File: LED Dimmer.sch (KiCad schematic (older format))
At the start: 78 parts, among them P1 Red Load, P2 Green Load, P3 Blue Load, P4 PWR, Q1 TIP31C, Q2 TIP31C, Q3 TIP31C, Q4 Q_PNP_EBC, Q5 Q_PNP_EBC, Q6 Q_NPN_EBC, SW1 SW_SPDT, SW10 SW_SPDT, SW11 SW_SPDT, SW12 SW_SPDT, SW2 SW_SPDT, SW3 SW_SPDT, SW4 SW_SPDT, SW5 SW_SPDT, SW6 SW_SPDT, SW7 SW_SPDT, SW8 SW_SPDT, SW9 SW_SPDT, U1 LM358, U2 LM358, U3 LM358, U4 LM555N

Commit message: Routed
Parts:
- R7: Power (none) -> 1/4W
- TP1, TP2, TP3, TP4, TP5, TP6, TP7, TP8: footprint LED Dimmer Footprints:Measurement_Point_Round-SMD-Pad_Big -> LED Dimmer Footprints:test_pt_alt
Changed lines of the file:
@@
 F 2 "LED Dimmer Footprints:R_Axial" V 2530 1900 50  0001 C CNN
 F 3 "" H 2600 1900 50  0000 C CNN
+F 4 "1/4W" V 2600 1900 60  0001 C CNN "Power"
 	1    2600 1900
 	0    1    1    0
@@
 F 0 "TP7" H 9000 2700 50  0000 C BNN
 F 1 "TEST" H 9000 2650 50  0000 C CNN
-F 2 "LED Dimmer Footprints:Measurement_Point_Round-SMD-Pad_Big" H 9000 2400 50  0001 C CNN
+F 2 "LED Dimmer Footprints:test_pt_alt" H 9000 2400 50  0001 C CNN
 F 3 "" H 9000 2400 50  0001 C CNN
 	1    9000 2400
@@
 F 0 "TP8" H 10400 5300 50  0000 C BNN
 F 1 "TEST" H 10400 5250 50  0000 C CNN
-F 2 "LED Dimmer Footprints:Measurement_Point_Round-SMD-Pad_Big" H 10400 5000 50  0001 C CNN
+F 2 "LED Dimmer Footprints:test_pt_alt" H 10400 5000 50  0001 C CNN
 F 3 "" H 10400 5000 50  0001 C CNN
 	1    10400 5000
@@
 F 0 "TP3" H 4050 6800 50  0000 C BNN
 F 1 "TEST" H 4050 6750 50  0000 C CNN
-F 2 "LED Dimmer Footprints:Measurement_Point_Round-SMD-Pad_Big" H 4050 6500 50  0001 C CNN
+F 2 "LED Dimmer Footprints:test_pt_alt" H 4050 6500 50  0001 C CNN
 F 3 "" H 4050 6500 50  0001 C CNN
 	1    4050 6500
@@
 F 0 "TP2" H 4050 4650 50  0000 C BNN
 F 1 "TEST" H 4050 4600 50  0000 C CNN
-F 2 "LED Dimmer Footprints:Measurement_Point_Round-SMD-Pad_Big" H 4050 4350 50  0001 C CNN
+F 2 "LED Dimmer Footprints:test_pt_alt" H 4050 4350 50  0001 C CNN
 F 3 "" H 4050 4350 50  0001 C CNN
 	1    4050 4350
@@
 F 0 "TP1" H 3900 1800 50  0000 C BNN
 F 1 "TEST" H 3900 1750 50  0000 C CNN
-F 2 "LED Dimmer Footprints:Measurement_Point_Round-SMD-Pad_Big" H 3900 1500 50  0001 C CNN
+F 2 "LED Dimmer Footprints:test_pt_alt" H 3900 1500 50  0001 C CNN
 F 3 "" H 3900 1500 50  0001 C CNN
 	1    3900 1500
@@
 F 0 "TP4" H 6150 1550 50  0000 C BNN
 F 1 "TEST" H 6150 1500 50  0000 C CNN
-F 2 "LED Dimmer Footprints:Measurement_Point_Round-SMD-Pad_Big" H 6150 1250 50  0001 C CNN
+F 2 "LED Dimmer Footprints:test_pt_alt" H 6150 1250 50  0001 C CNN
 F 3 "" H 6150 1250 50  0001 C CNN
 	1    6150 1250
@@
 F 0 "TP5" H 6200 3750 50  0000 C BNN
 F 1 "TEST" H 6200 3700 50  0000 C CNN
-F 2 "LED Dimmer Footprints:Measurement_Point_Round-SMD-Pad_Big" H 6200 3450 50  0001 C CNN
+F 2 "LED Dimmer Footprints:test_pt_alt" H 6200 3450 50  0001 C CNN
 F 3 "" H 6200 3450 50  0001 C CNN
 	1    6200 3450
@@
 F 0 "TP6" H 6200 5900 50  0000 C BNN
 F 1 "TEST" H 6200 5850 50  0000 C CNN
-F 2 "LED Dimmer Footprints:Measurement_Point_Round-SMD-Pad_Big" H 6200 5600 50  0001 C CNN
+F 2 "LED Dimmer Footprints:test_pt_alt" H 6200 5600 50  0001 C CNN
 F 3 "" H 6200 5600 50  0001 C CNN
 	1    6200 5600

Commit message: Renamed library for compatibility with 3D viewer
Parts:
- C1: footprint LED Dimmer Footprints:C_Disc -> led_dimmer_footprints:C_Disc
- D1: footprint LED Dimmer Footprints:LED_D5.0mm-4 -> led_dimmer_footprints:LED_D5.0mm-4
- D2: footprint LED Dimmer Footprints:D_axial -> led_dimmer_footprints:D_axial
- P1, P2, P3, P4: footprint LED Dimmer Footprints:2.1ID_5.5OD_SIDE_MOUNT_JACK -> led_dimmer_footprints:2.1ID_5.5OD_SIDE_MOUNT_JACK
- Q1, Q2, Q3: footprint LED Dimmer Footprints:TO-220_Vertical -> led_dimmer_footprints:TO-220_Vertical
- Q4, Q5, Q6: footprint LED Dimmer Footprints:TO-92_Molded_Wide -> led_dimmer_footprints:TO-92_Molded_Wide
- R1, R10, R11, R12, R13, R14, R15, R16, R17, R18, R19, R2, R20, R21, R22, R23, R24, R25, R26, R27, R28, R29, R3, R30, R31, R32, R33, R34, R35, R36, R37, R38, R39, R4, R40, R5, R6, R7, R8, R9: footprint LED Dimmer Footprints:R_Axial -> led_dimmer_footprints:R_Axial
- RV1: footprint LED Dimmer Footprints:POT_UM_296RE -> led_dimmer_footprints:POT_UM_296RE
- SW1, SW10, SW11, SW12, SW2, SW3, SW4, SW5, SW6, SW7, SW8, SW9: footprint LED Dimmer Footprints:SW_SPDT_PCBPM -> led_dimmer_footprints:SW_SPDT_PCBPM
- TP1, TP2, TP3, TP4, TP5, TP6, TP7, TP8: footprint LED Dimmer Footprints:test_pt_alt -> led_dimmer_footprints:test_pt_alt
- U1, U2, U3: footprint LED Dimmer Footprints:DIP8_dualopamp -> led_dimmer_footprints:DIP8_dualopamp
- U4: footprint LED Dimmer Footprints:DIP8 -> led_dimmer_footprints:DIP8

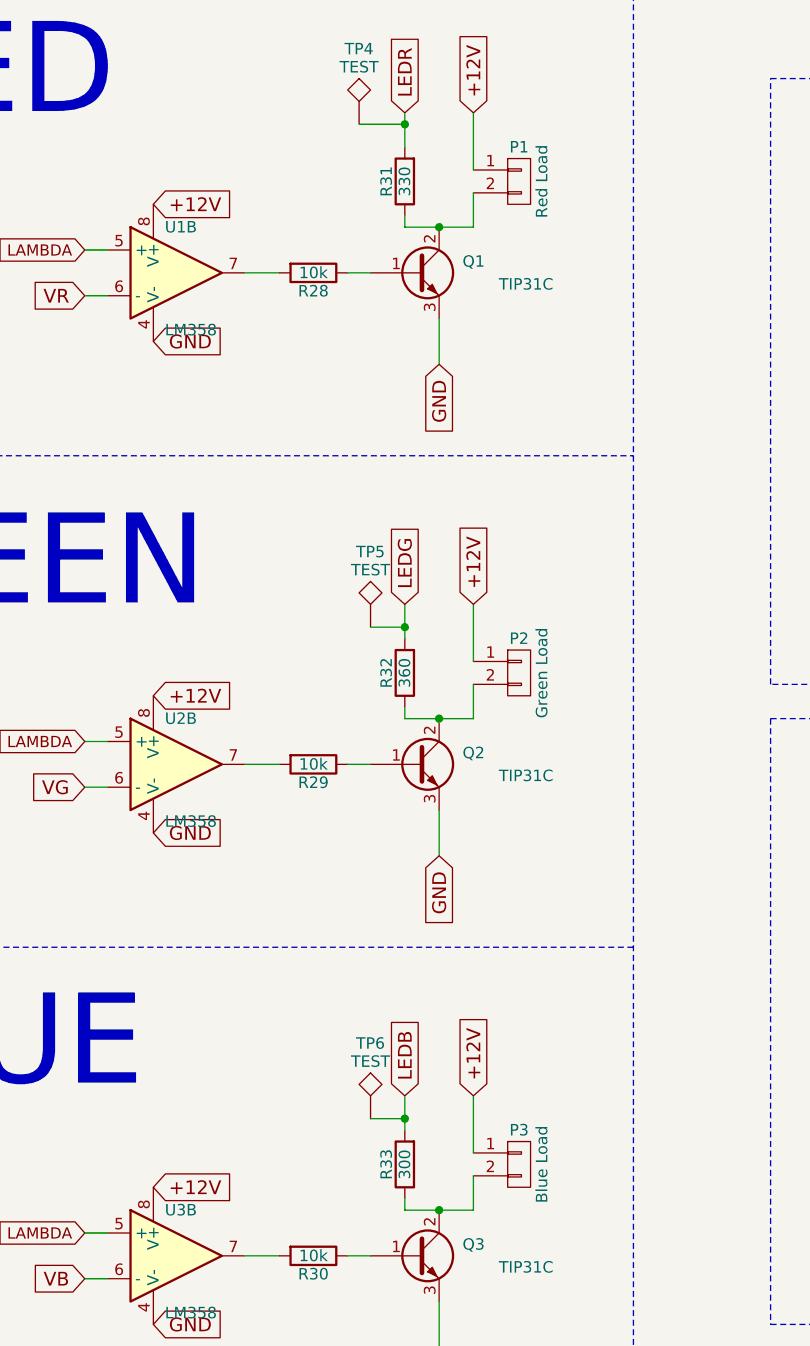
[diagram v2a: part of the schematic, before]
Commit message: Added RED/GREEN/BLUE text to silkscreen, changed load resistor values to be a bit more conservative
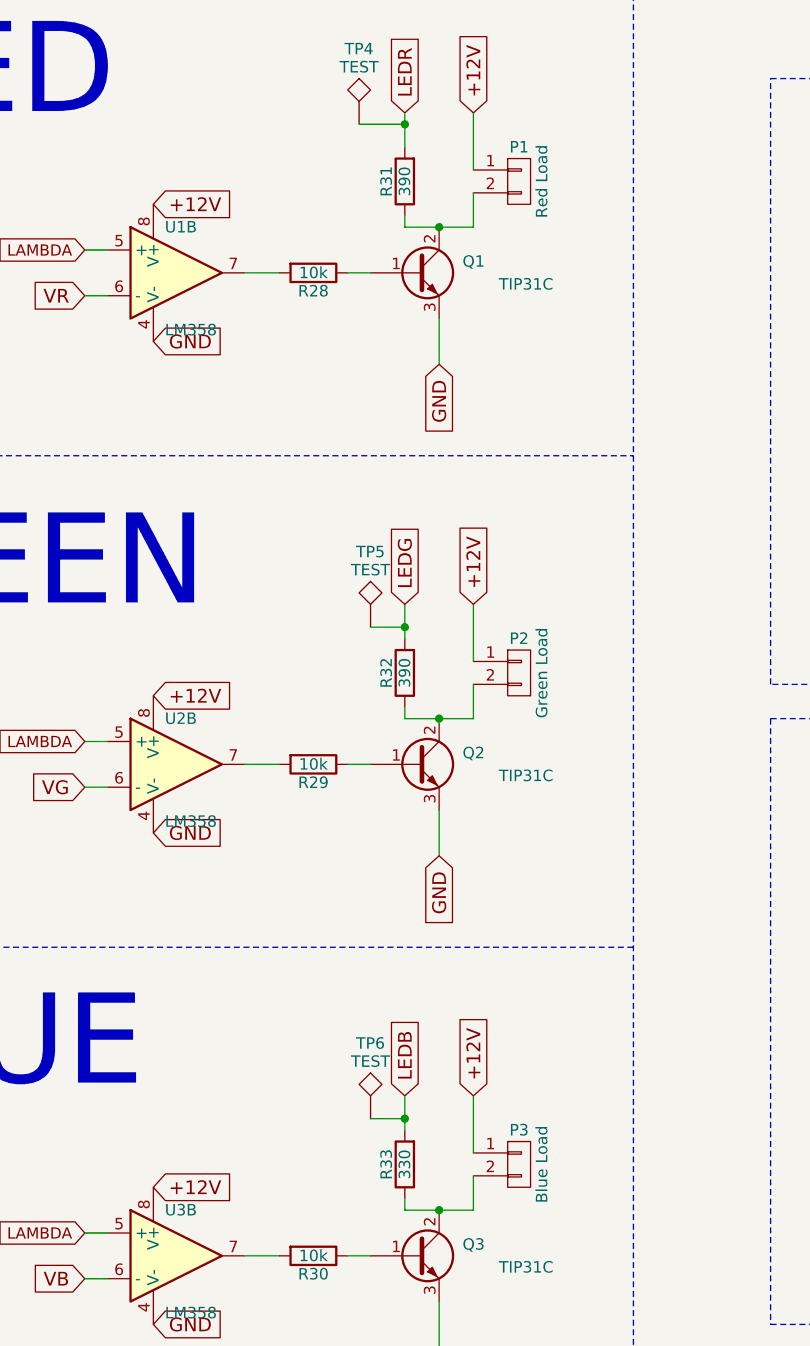
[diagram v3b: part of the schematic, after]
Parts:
- R31: value 330 -> 390
- R32: value 360 -> 390
- R33: value 300 -> 330
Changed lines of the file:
@@
 P 6350 1500
 F 0 "R31" V 6430 1500 50  0000 C CNN
-F 1 "330" V 6350 1500 50  0000 C CNN
+F 1 "390" V 6350 1500 50  0000 C CNN
 F 2 "led_dimmer_footprints:R_Axial" V 6280 1500 50  0001 C CNN
 F 3 "" H 6350 1500 50  0000 C CNN
@@
 P 6350 3650
 F 0 "R32" V 6430 3650 50  0000 C CNN
-F 1 "360" V 6350 3650 50  0000 C CNN
+F 1 "390" V 6350 3650 50  0000 C CNN
 F 2 "led_dimmer_footprints:R_Axial" V 6280 3650 50  0001 C CNN
 F 3 "" H 6350 3650 50  0000 C CNN
@@
 P 6350 5800
 F 0 "R33" V 6430 5800 50  0000 C CNN
-F 1 "300" V 6350 5800 50  0000 C CNN
+F 1 "330" V 6350 5800 50  0000 C CNN
 F 2 "led_dimmer_footprints:R_Axial" V 6280 5800 50  0001 C CNN
 F 3 "" H 6350 5800 50  0000 C CNN
